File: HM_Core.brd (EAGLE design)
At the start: 45.7 x 61 mm, 7 parts

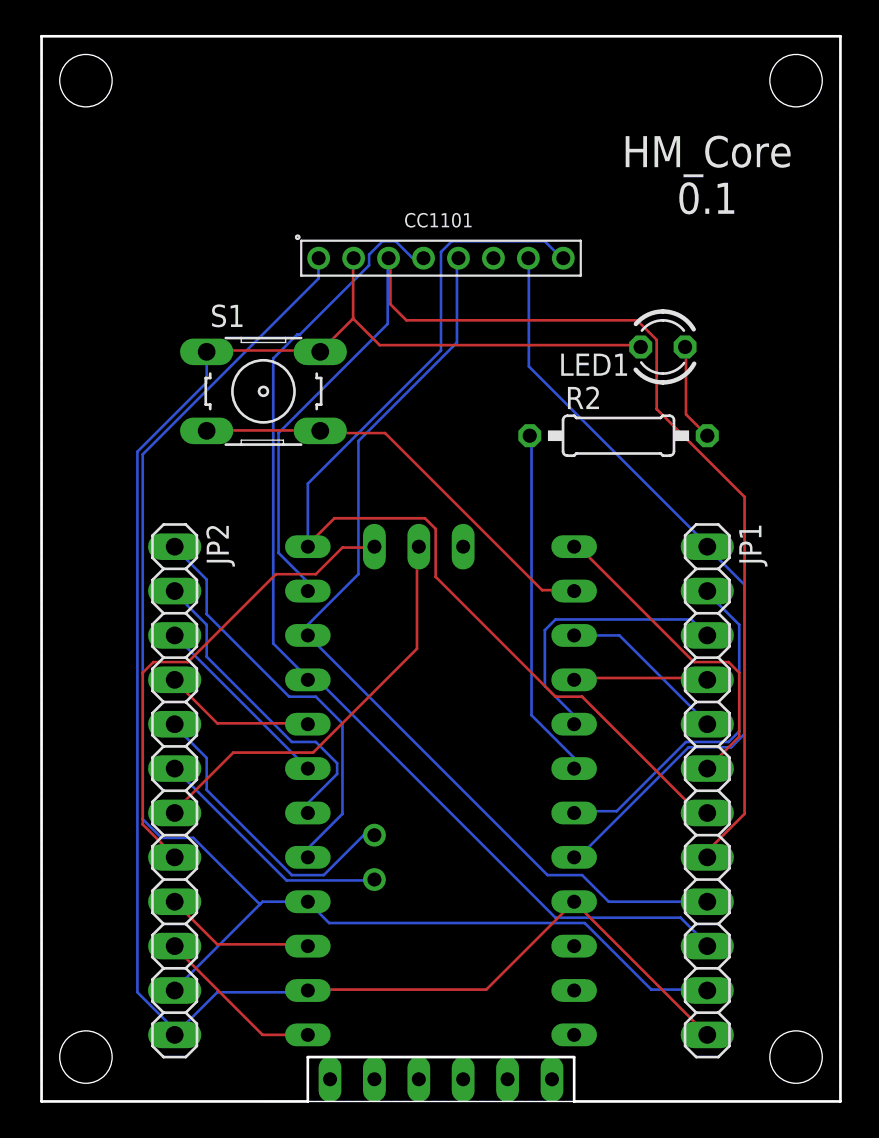
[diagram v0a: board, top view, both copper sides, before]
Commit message: Verbesserungen
Taster zur seite raus
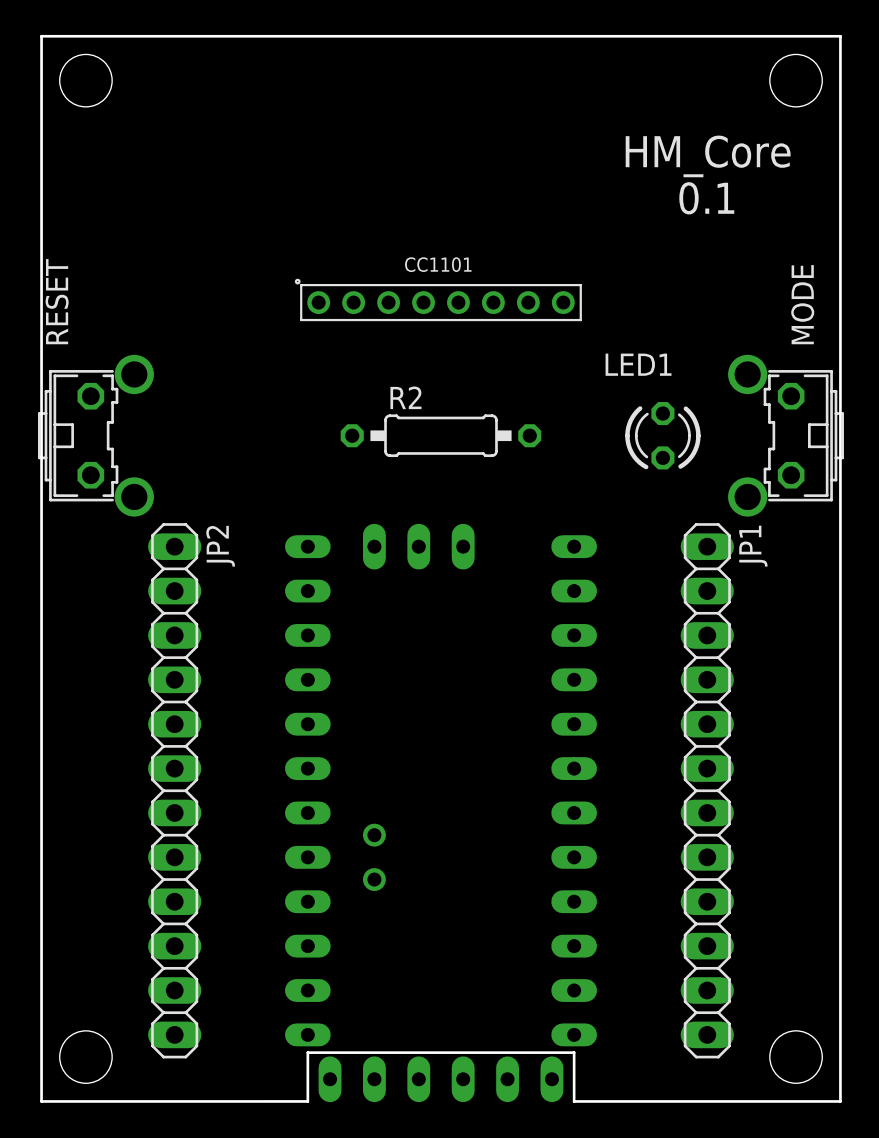
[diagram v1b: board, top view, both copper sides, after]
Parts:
- removed S1: (no value), switch-omron:B3F-10XX
- added MODE: Mode, switch-omron:B3F-31XX
- added RESET: Reset, switch-omron:B3F-31XX
- moved R2 10.2 mm to (22.9, 38.1)
- moved LED1 5.08 mm to (35.6, 38.1), turned to 90 degrees
- moved CC1101 2.54 mm to (22.9, 45.7)
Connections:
- net D8: now also MODE.2; no longer S1.3, S1.4
- net GND: now also MODE.1, RESET.2; no longer S1.1, S1.2
- net RST: now also RESET.1
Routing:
- net GND: track 108.3 -> 0.22 mm
- net VCC: track 79.7 -> 0.05 mm
- net D11: track 73.7 -> 0.00 mm
- net D13: track 60.6 -> 0.00 mm
- net D10: track 59.9 -> 0.00 mm
- net D12: track 54.3 -> 0.00 mm
- net D2: track 45.1 -> 0.46 mm
- net A7: track 27.6 -> 0.00 mm
- net D8: track 24.9 -> 0.00 mm
- net A6: track 23.7 -> 0.00 mm
- net A0: track 23.5 -> 0.00 mm
- net D3: track 20.2 -> 0.10 mm
- net D4: track 20.2 -> 0.61 mm
- net D9: track 18.7 -> 0.00 mm
- net A1: track 18.0 -> 0.00 mm
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- removed copper zone on layer 16, net GND
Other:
- outline, holes or cut-outs redrawn
